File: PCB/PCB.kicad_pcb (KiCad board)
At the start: 2 copper layers, 60.7 x 60.7 mm, 60 parts, among them IC1 ESP32-C6-WROOM-1-N8, J1 USB_C_Receptacle_USB2.0_14P, J2 USB_C_Receptacle_USB2.0_14P, J3 Conn_01x04, J5 Jumper CAN, J8 Aux_IMU, SW1 TK-6580A8-1, SW2 TK-6580A8-1, U1 CP2102N-Axx-xQFN28, U2 AMS1117-3.3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

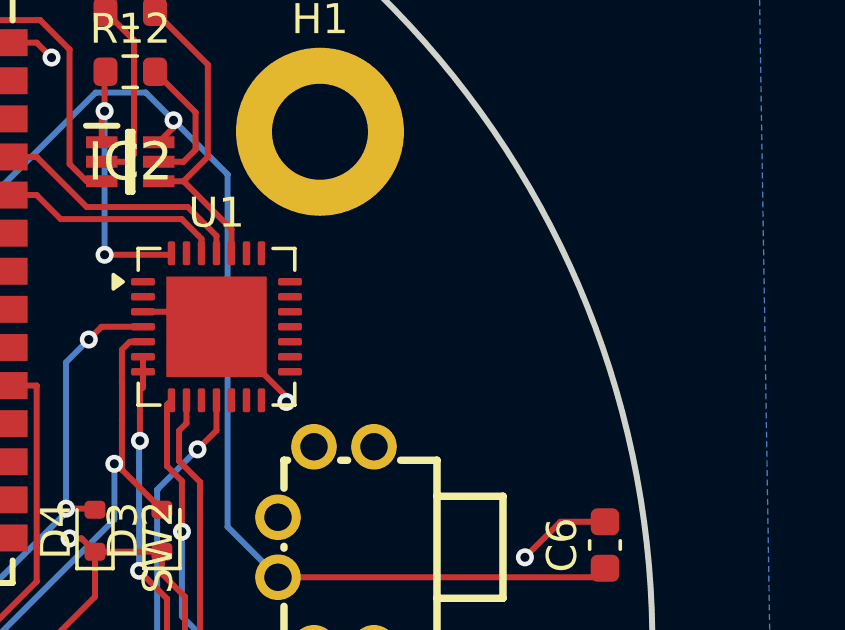
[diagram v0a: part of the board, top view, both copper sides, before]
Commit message: Se incorpora logo y se regeneran ficheros de producción
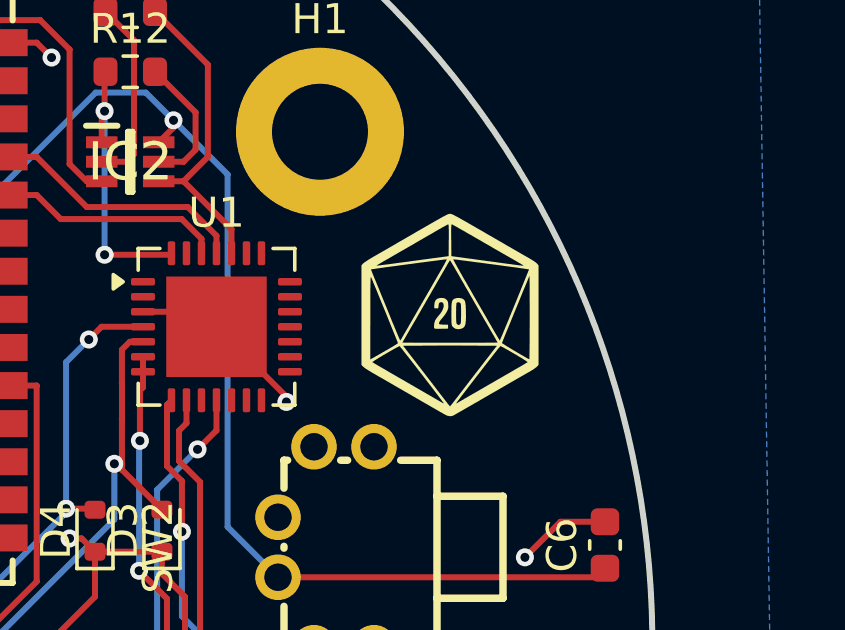
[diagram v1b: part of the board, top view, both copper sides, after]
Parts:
- added G2: LOGO, LOGO, F.Cu at (188.5, 74.0)
- renumbered G*** to G1
